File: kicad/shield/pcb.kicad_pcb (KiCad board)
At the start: 2 copper layers, 48.9 x 49.5 mm, 15 parts, among them J1 Conn_01x12_Fem_l, J2 Conn_01x12_Fem_r, J3 Conn_01x12_Fem_b_r, J4 Conn_01x09_Fem_b_l

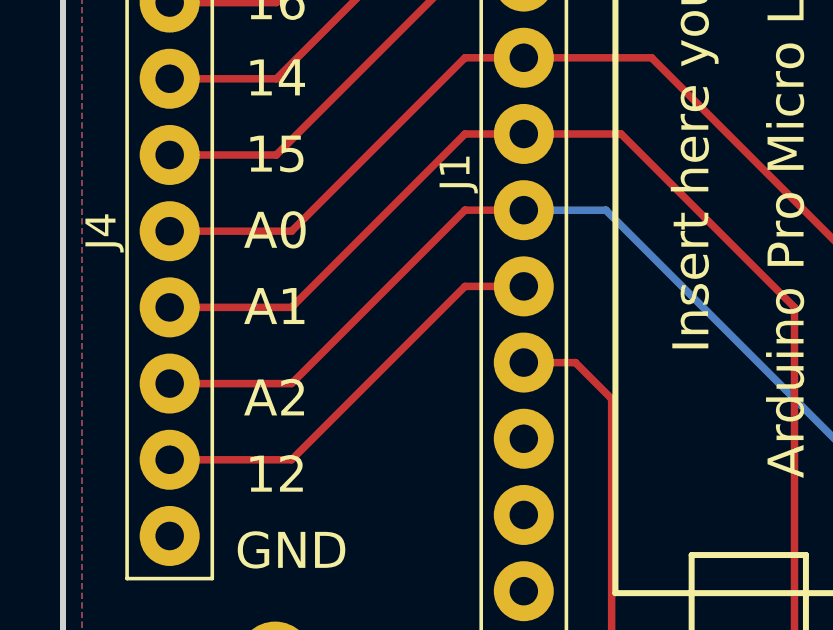
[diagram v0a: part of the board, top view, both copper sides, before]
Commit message: updates
- print the front and back copper layer to check the connections
- add silks pictures
- ready to print first prototype
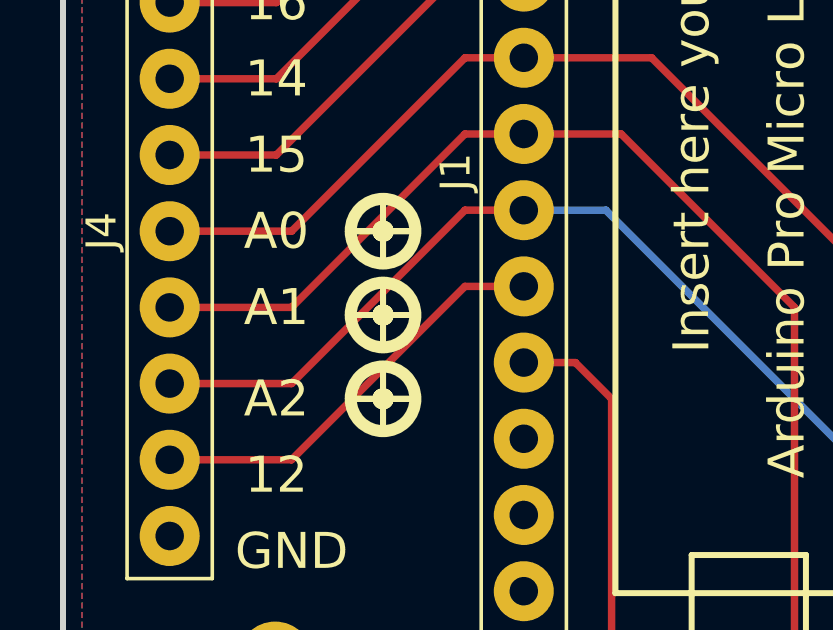
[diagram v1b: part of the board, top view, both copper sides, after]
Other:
- board text added: "Play your simulation games with"
- board text added: "USB HID device Plug and Play Small and Cute :)"
- board text added: "Volante"

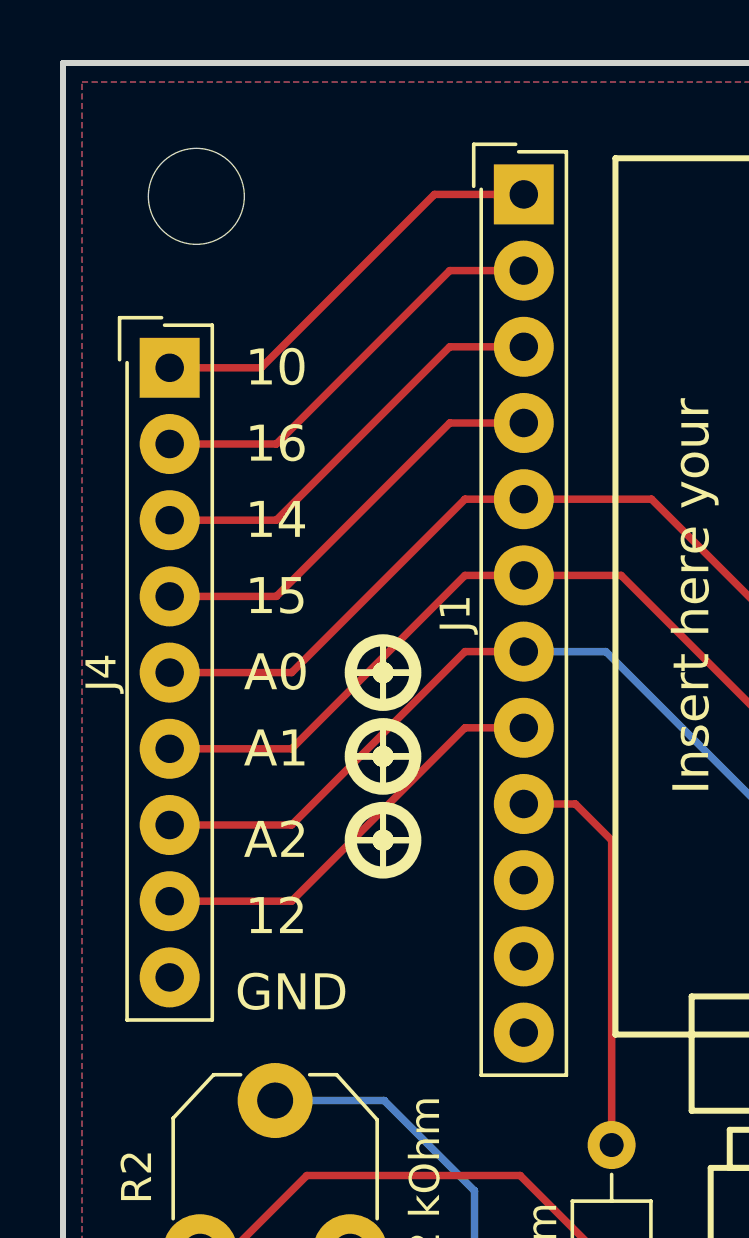
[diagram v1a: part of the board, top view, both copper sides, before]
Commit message: VCC pin
- add Vcc pin
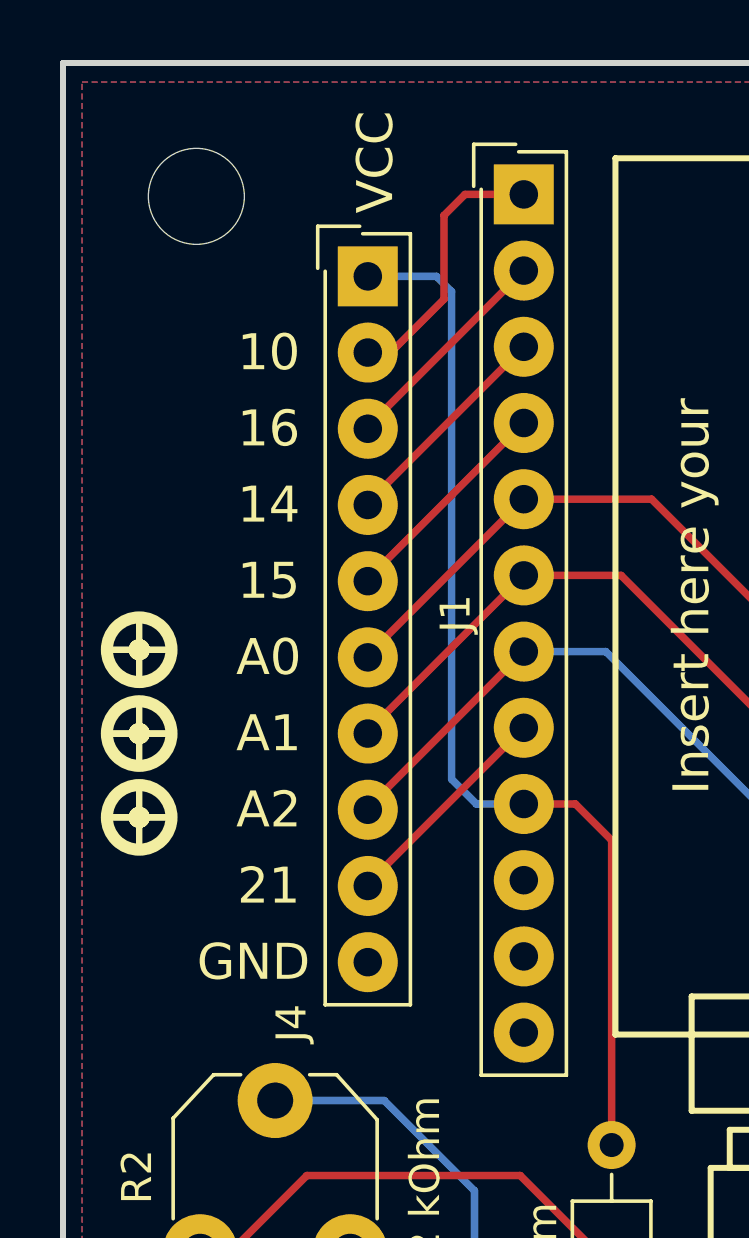
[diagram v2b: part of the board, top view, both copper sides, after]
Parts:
- J4: footprint Connectors_Samtec:SL-109-X-XX_1x09 -> Connectors_Samtec:SL-110-X-XX_1x10
- moved J4 7.27 mm to (99.1, 68.1)
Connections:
- J1 pad 9: Net-(J1-Pad9) -> VCC
- J4 pad 1: 10 -> VCC
- J4 pad 2: 16 -> 10
- J4 pad 3: 14 -> 16
- J4 pad 4: 15 -> 14
- J4 pad 5: A0 -> 15
- J4 pad 6: A1 -> A0
- J4 pad 7: A2 -> A1
- J4 pad 8: 21 -> A2
- J4 pad 9: GND -> 21
- R1 pad 1: Net-(J1-Pad9) -> VCC
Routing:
- net VCC: track 0.00 -> 35.6 mm
- net Net-(J1-Pad9): track 13.6 -> 0.00 mm
- net 14: track 14.2 -> 7.43 mm
- net 21: track 14.2 -> 7.43 mm
- net A0: track 53.0 -> 46.2 mm
- net 16: track 14.2 -> 7.43 mm
- net 15: track 14.2 -> 7.43 mm
- net A2: track 44.8 -> 38.0 mm
- net A1: track 44.4 -> 37.7 mm
- net 10: track 14.2 -> 9.02 mm
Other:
- board text added: "21"
- board text added: "VCC"
- board text removed: "12"
